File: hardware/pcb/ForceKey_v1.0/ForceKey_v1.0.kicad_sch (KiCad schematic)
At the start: 25 parts, among them CN1 PJ-320A, J1 PINHD_1x2_Male, J2 PINHD_1x4_Male, J3 PINHD_1x4_Male, J4 PINHD_1x5_Male, Q1 BC817-40W, Q2 BC817-40W, Q3 BC817-40W, U1 PY32F002AL15S6TU, U2 ME6211C33M5, U3 PJ4054B

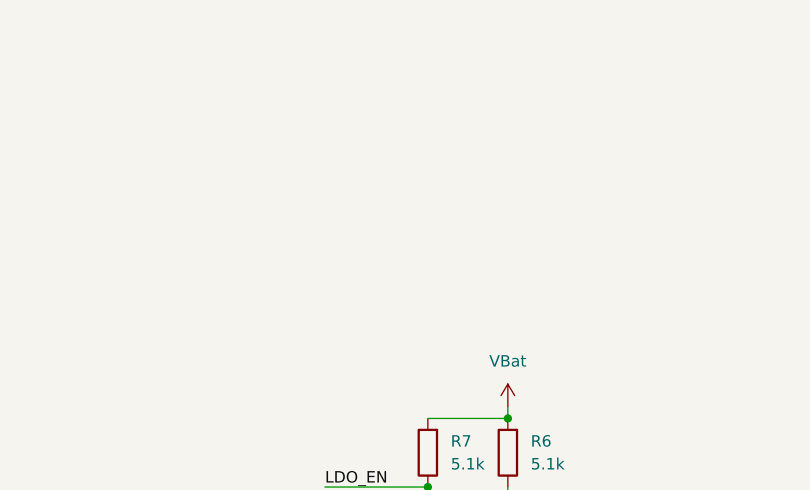
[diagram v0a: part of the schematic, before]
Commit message: added switch & basic PCB layout draft
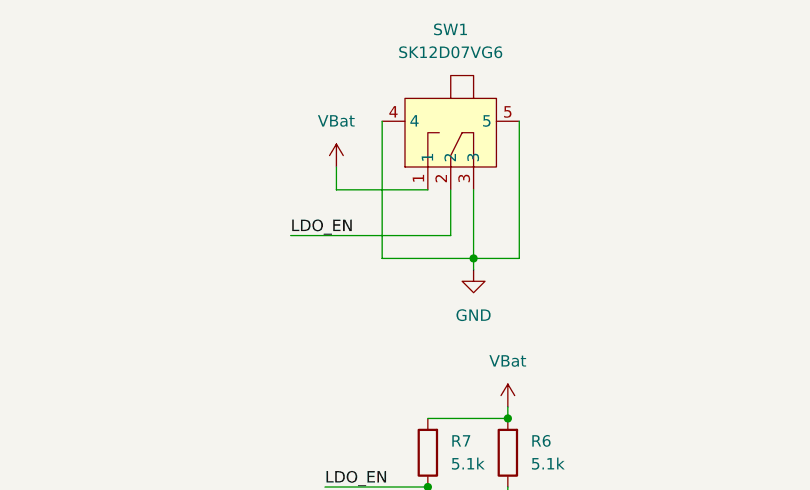
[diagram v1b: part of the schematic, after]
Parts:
- added SW1: SK12D07VG6, SK12D07VG6:SW-TH_SK12D07VG6, symbol SK12D07VG6:SK12D07VG6
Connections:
- net GND: now also SW1.3, SW1.4, SW1.5
- net LDO_EN: now also SW1.2
- net VBat: now also SW1.1

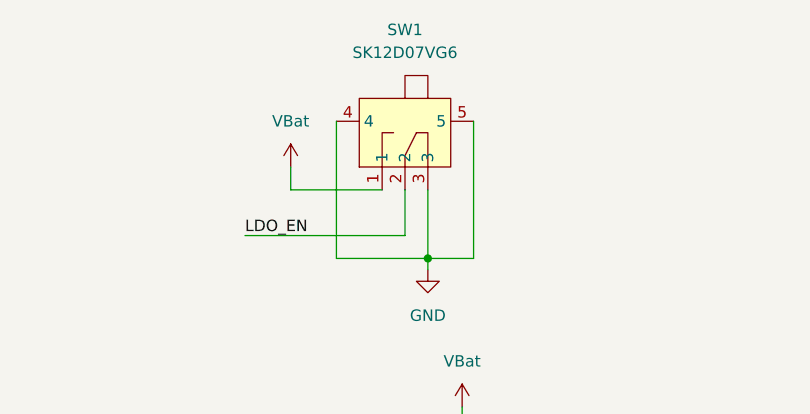
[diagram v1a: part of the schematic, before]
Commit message: added power traces, updated footprints
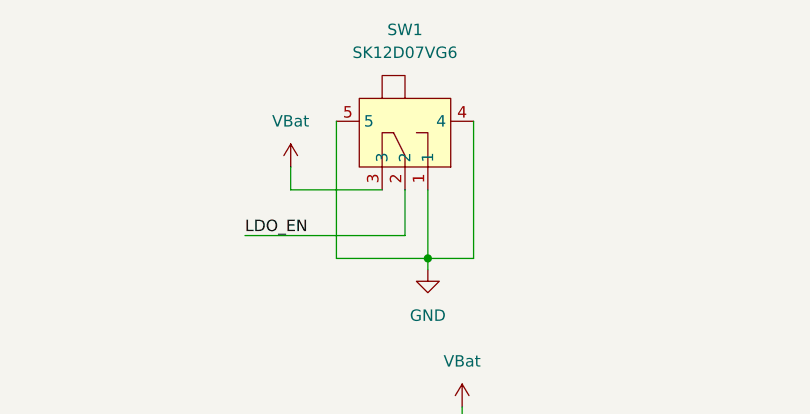
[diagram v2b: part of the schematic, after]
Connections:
- net GND: now also SW1.1; no longer SW1.3
- net VBat: now also SW1.3; no longer SW1.1
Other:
- moved on the sheet: SW1
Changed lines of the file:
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@@
+	(wire
+		(pts
+			(xy 135.89 127) (xy 129.54 127)
+		)
+		(stroke
+			(width 0)
+			(type default)
+		)
+	)
+	(wire
+		(pts
+			(xy 199.39 34.29) (xy 199.39 36.83)
+		)
+		(stroke
+			(width 0)
+			(type default)
+		)
+	)
+	(wire
+		(pts
+			(xy 48.26 38.1) (xy 49.53 38.1)
+		)
+		(stroke
+			(width 0)
+			(type default)
+		)
+	)
+	(wire
+		(pts
+			(xy 49.53 30.48) (xy 49.53 38.1)
+		)
+		(stroke
+			(width 0)
+			(type default)
+		)
+	)
+	(wire
+		(pts
+			(xy 129.54 115.57) (xy 132.08 115.57)
+		)
+		(stroke
+			(width 0)
+			(type default)
+		)
+	)
+	(wire
+		(pts
+			(xy 100.33 99.06) (xy 100.33 100.33)
+		)
+		(stroke
+			(width 0)
+			(type default)
+		)
+	)
+	(wire
+		(pts
+			(xy 54.61 151.13) (xy 54.61 154.94)
+		)
+		(stroke
+			(width 0)
+			(type default)
+		)
+	)
+	(wire
+		(pts
+			(xy 54.61 27.94) (xy 54.61 33.02)
+		)
+		(stroke
+			(width 0)
+			(type default)
+		)
+	)
+	(wire
+		(pts
+			(xy 129.54 104.14) (xy 129.54 101.6)
+		)
+		(stroke
+			(width 0)
+			(type default)
+		)
+	)
+	(wire
+		(pts
+			(xy 93.98 115.57) (xy 106.68 115.57)
+		)
+		(stroke
+			(width 0)
+			(type default)
+		)
+	)
+	(wire
+		(pts
+			(xy 40.64 162.56) (xy 40.64 165.1)
+		)
+		(stroke
+			(width 0)
+			(type default)
+		)
+	)
 	(wire
 		(pts
@@
 	(wire
 		(pts
-			(xy 135.89 127) (xy 129.54 127)
+			(xy 25.4 113.03) (xy 43.18 113.03)
 		)
 		(stroke
@@
 	(wire
 		(pts
-			(xy 199.39 34.29) (xy 199.39 36.83)
+			(xy 142.24 48.26) (xy 142.24 49.53)
 		)
 		(stroke
@@
 	(wire
 		(pts
-			(xy 48.26 38.1) (xy 49.53 38.1)
+			(xy 43.18 113.03) (xy 43.18 115.57)
 		)
 		(stroke
@@
 	(wire
 		(pts
-			(xy 49.53 30.48) (xy 49.53 38.1)
+			(xy 16.51 153.67) (xy 33.02 153.67)
 		)
 		(stroke
@@
 		)
 	)
-	(wire
-		(pts
-			(xy 129.54 115.57) (xy 132.08 115.57)
-		)
-		(stroke
-			(width 0)
-			(type default)
-		)
-	)
-	(wire
-		(pts
-			(xy 100.33 99.06) (xy 100.33 100.33)
-		)
-		(stroke
-			(width 0)
-			(type default)
-		)
-	)
-	(wire
-		(pts
-			(xy 54.61 151.13) (xy 54.61 154.94)
-		)
-		(stroke
-			(width 0)
-			(type default)
-		)
-	)
-	(wire
-		(pts
-			(xy 54.61 27.94) (xy 54.61 33.02)
-		)
-		(stroke
-			(width 0)
-			(type default)
-		)
-	)
-	(wire
-		(pts
-			(xy 129.54 104.14) (xy 129.54 101.6)
-		)
-		(stroke
-			(width 0)
-			(type default)
-		)
-	)
-	(wire
-		(pts
-			(xy 93.98 115.57) (xy 106.68 115.57)
-		)
-		(stroke
-			(width 0)
-			(type default)
-		)
-	)
-	(wire
-		(pts
-			(xy 40.64 162.56) (xy 40.64 165.1)
-		)
-		(stroke
-			(width 0)
-			(type default)
-		)
-	)
-	(wire
-		(pts
-			(xy 25.4 113.03) (xy 43.18 113.03)
-		)
-		(stroke
-			(width 0)
-			(type default)
-		)
-	)
-	(wire
-		(pts
-			(xy 142.24 48.26) (xy 142.24 49.53)
-		)
-		(stroke
-			(width 0)
-			(type default)
-		)
-	)
-	(wire
-		(pts
-			(xy 43.18 113.03) (xy 43.18 115.57)
-		)
-		(stroke
-			(width 0)
-			(type default)
-		)
-	)
-	(wire
-		(pts
-			(xy 16.51 153.67) (xy 33.02 153.67)
-		)
-		(stroke
-			(width 0)
-			(type default)
-		)
-	)
 	(label "LDO_EN"
 		(at 194.31 41.91 0)
@@
 	(symbol
 		(lib_id "SK12D07VG6:SK12D07VG6")
-		(at 212.09 31.75 0)
-		(mirror x)
-		(unit 1)
-		(exclude_from_sim no)
-		(in_bom yes)
-		(on_board yes)
-		(dnp no)
-		(fields_autoplaced yes)
+		(at 212.09 31.75 180)
+		(unit 1)
+		(exclude_from_sim no)
+		(in_bom yes)
+		(on_board yes)
+		(dnp no)
 		(property "Reference" "SW1"
 			(at 212.09 19.05 0)

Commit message: Finished Schematic and PCB
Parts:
- removed J4: PINHD_1x5_Male, Connector_PinHeader_2.54mm:PinHeader_1x05_P2.54mm_Vertical, symbol PCM_SL_Pin_Headers:PINHD_1x5_Male
- added J4: Conn_ARM_SWD_TagConnect_TC2030-NL, Connector:Tag-Connect_TC2030-IDC-NL_2x03_P1.27mm_Vertical, symbol Connector:Conn_ARM_SWD_TagConnect_TC2030-NL
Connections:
- net +3.3V: now also J4.1 (VCC)
- net DASH: now also U1.7 (PA1); no longer U1.4 (PA14-SWC/PB3)
- net DOT: now also J4.2 (SWDIO)
- net GND: now also J4.5 (GND)
- net RST: now also J4.3 (~{RESET})
- net SCK: now reaches U1.2 (PA4/PA10)
- net SCK: now also J2.2, J3.2
- net LEFT_DIO: now reaches U1.3 (PA3)
- net LEFT_DIO: now also J2.3
- net RIGHT_DIO: now reaches J3.3
- net RIGHT_DIO: now also U1.4 (PA14-SWC/PB3), J4.4 (SWCLK)
- no-connect marks 0 -> 7
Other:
- moved on the sheet: C1, C6, J2, J3, U1
